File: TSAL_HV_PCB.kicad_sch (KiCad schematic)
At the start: 42 parts, among them J3 Conn_01x03_Socket, J4 Conn_01x03_Socket, K1 SPU01M-5, Q2 2N7002, Q3 2N7002, U1 LM393, U2 4N35, U3 TPS7B88-Q1

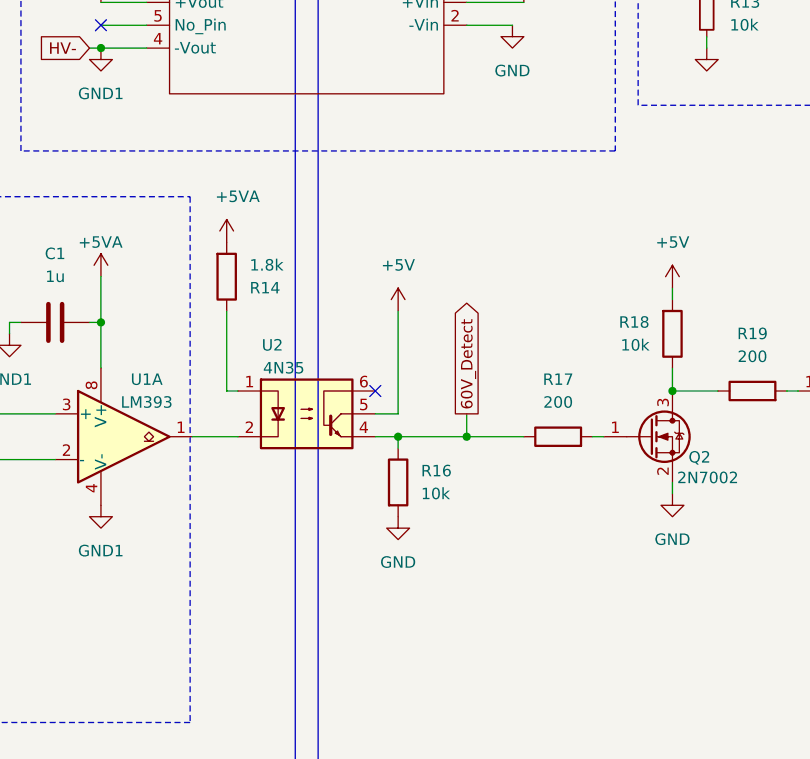
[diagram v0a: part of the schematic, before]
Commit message: *: Add series resistor and pull-down to optocoupler BJT
The series resistor protects against shorts on the output and the base
pull-down helps with noise immunity.
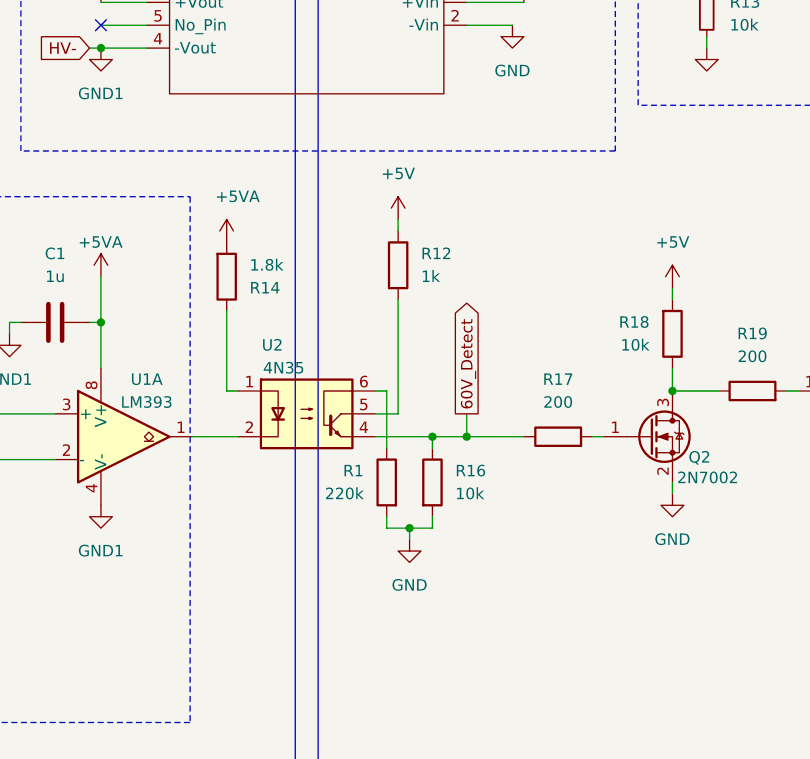
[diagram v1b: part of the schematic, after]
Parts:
- added R1: 220k, Resistor_SMD:R_0603_1608Metric, symbol Device:R
- added R12: 1k, Resistor_SMD:R_0603_1608Metric, symbol Device:R
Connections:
- net +5V: now also R12.1; no longer U2.5
- net GND: now also R1.2
- net at U2.6: now also R1.1
- new net: R12.2, U2.5
- no-connect marks 3 -> 2
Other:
- moved on the sheet: R16
